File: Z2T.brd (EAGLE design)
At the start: 36 x 64 mm, 9 parts, among them J1 M02X7-SOCKET, J2 M02X6-SOCKET

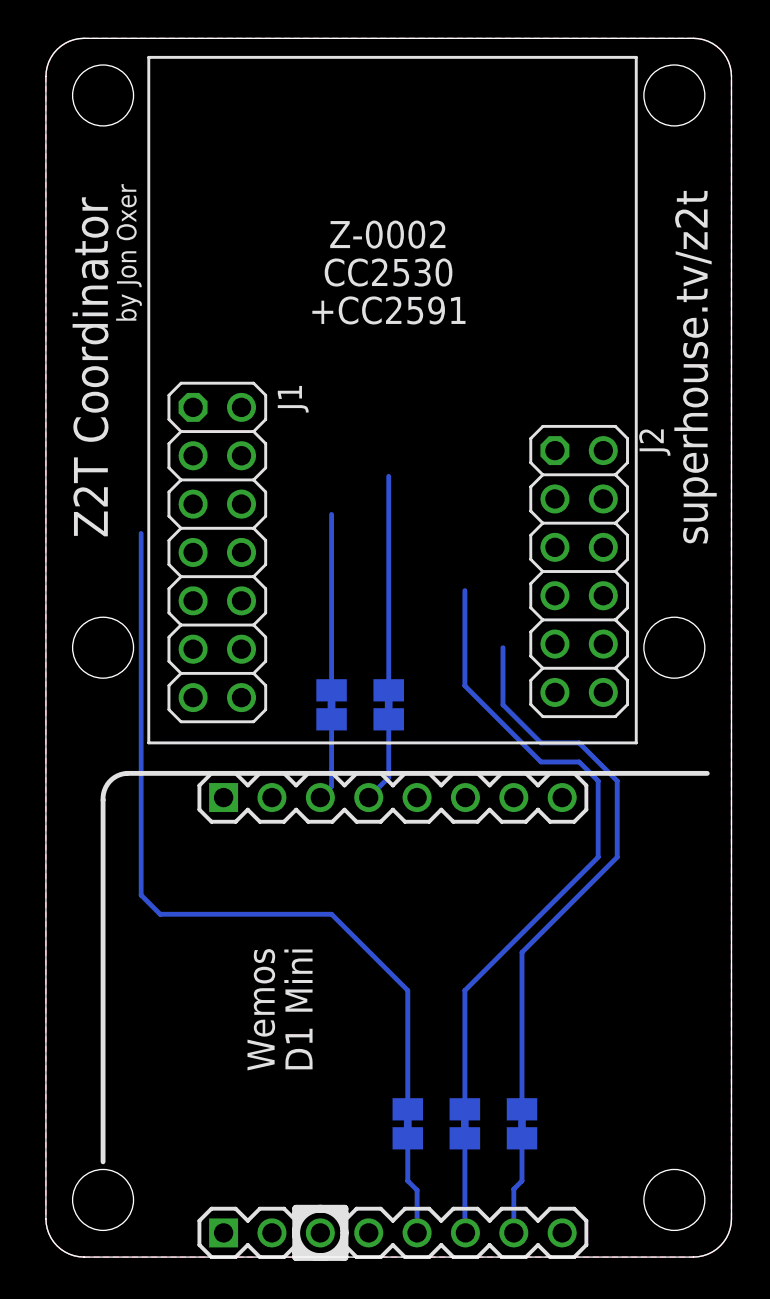
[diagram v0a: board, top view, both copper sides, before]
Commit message: Mechanical adjustments on Zigbee module
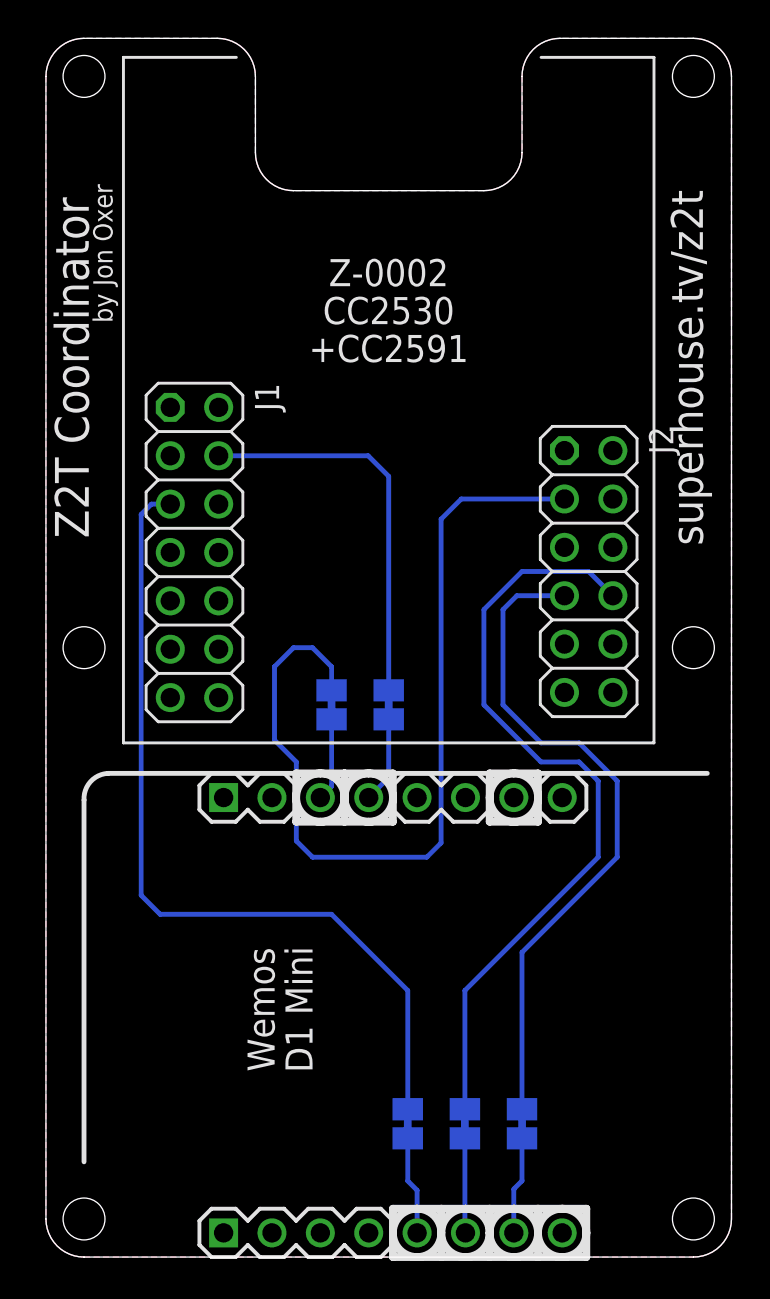
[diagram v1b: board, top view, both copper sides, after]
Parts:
- moved J1 1.20 mm to (7.80, 37.0)
- moved J2 0.50 mm to (28.5, 36.0)
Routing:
- net CC_RST: track 9.24 -> 46.9 mm
- net P2_2_DC: track 11.2 -> 20.6 mm
- net P0_3: track 34.2 -> 40.9 mm
- net P0_2: track 30.0 -> 35.5 mm
- net P2_1_DD: track 41.3 -> 44.1 mm
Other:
- outline, holes or cut-outs redrawn
- board text added: "D6: CC_DD D2: CC_DC D1: CC_RST D7: P0_3 D8: P0_2"
- board text added: "Released under the terms of the TAPR Open Hardware License: tapr.org/OHL"

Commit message: Final routing, silkscreen, DRC, and docs for v1.0 release
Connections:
- removed net 5V: J4.8
- removed net A0: J3.2
- removed net D0: J3.3
- removed net D3: J4.5
- removed net D4: J4.6
- removed net D5: J3.4
- removed net RST: J3.1
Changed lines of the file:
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@@
 <drawing>
 <settings>
-<setting alwaysvectorfont="yes"/>
+<setting alwaysvectorfont="no"/>
 <setting keepoldvectorfont="yes"/>
 <setting verticaltext="up"/>
@@
 <wire x1="18" y1="25.18" x2="18" y2="28.238" width="0.254" layer="16"/>
 </signal>
-<signal name="D5">
-<contactref element="J3" pad="4"/>
-</signal>
 <signal name="D6">
 <contactref element="J3" pad="5"/>
@@
 <wire x1="25" y1="4" x2="25" y2="6.238" width="0.254" layer="16"/>
 </signal>
-<signal name="A0">
-<contactref element="J3" pad="2"/>
-</signal>
-<signal name="D0">
-<contactref element="J3" pad="3"/>
-</signal>
-<signal name="D3">
-<contactref element="J4" pad="5"/>
-</signal>
-<signal name="D4">
-<contactref element="J4" pad="6"/>
-</signal>
 <signal name="RX">
 <contactref element="J4" pad="2"/>
@@
 <signal name="TX">
 <contactref element="J4" pad="1"/>
-</signal>
-<signal name="RST">
-<contactref element="J3" pad="1"/>
 </signal>
 <signal name="P2_3">
@@
 <contactref element="J2" pad="10"/>
 </signal>
-<signal name="5V">
-<contactref element="J4" pad="8"/>
-</signal>
 </signals>

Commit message: Fixed spacing on Zigbee module headers
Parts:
- moved J2 0.50 mm to (28.0, 36.0)
- moved J1 0.20 mm to (8.00, 37.0)
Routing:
- net P0_2: track 35.5 -> 35.0 mm
- net CC_RST: track 46.9 -> 46.4 mm
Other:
- board text added: "v1.1"
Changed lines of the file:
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@@
 <wire x1="4.07" y1="63" x2="10" y2="63" width="0.1524" layer="21"/>
 <wire x1="26" y1="63" x2="31.93" y2="63" width="0.1524" layer="21"/>
+<text x="4.712" y="7.24" size="1.27" layer="22" font="vector" ratio="18" rot="MR180" align="bottom-center">v1.1</text>
+<wire x1="35.84" y1="4.4" x2="29.73" y2="4.4" width="0.254" layer="21"/>
+<wire x1="27.84" y1="2.4" x2="29.73" y2="4.4" width="0.254" layer="21"/>
 </plain>
 <attributes>
@@
 <attribute name="VALUE" x="8.06" y="20.955" size="1.27" layer="27"/>
 </element>
-<element name="J2" library="SuperHouse-Connectors" library_urn="urn:adsk.eagle:library:11765989" package="2X06-S" package3d_urn="urn:adsk.eagle:package:15060598/2" value="M02X6-SOCKET" x="28.5" y="36" smashed="yes" rot="R270">
-<attribute name="NAME" x="31.675" y="43.62" size="1.27" layer="25" ratio="10" rot="R270"/>
-<attribute name="VALUE" x="24.055" y="43.62" size="1.27" layer="27" rot="R270"/>
-</element>
-<element name="J1" library="SuperHouse-Connectors" library_urn="urn:adsk.eagle:library:11765989" package="2X07-S" package3d_urn="urn:adsk.eagle:package:15060619/2" value="M02X7-SOCKET" x="7.8" y="37" smashed="yes" rot="R270">
-<attribute name="NAME" x="10.975" y="45.89" size="1.27" layer="25" ratio="10" rot="R270"/>
-<attribute name="VALUE" x="3.355" y="45.89" size="1.27" layer="27" rot="R270"/>
+<element name="J2" library="SuperHouse-Connectors" library_urn="urn:adsk.eagle:library:11765989" package="2X06-S" package3d_urn="urn:adsk.eagle:package:15060598/2" value="M02X6-SOCKET" x="28" y="36" smashed="yes" rot="R270">
+<attribute name="NAME" x="31.175" y="43.62" size="1.27" layer="25" ratio="10" rot="R270"/>
+<attribute name="VALUE" x="23.555" y="43.62" size="1.27" layer="27" rot="R270"/>
+</element>
+<element name="J1" library="SuperHouse-Connectors" library_urn="urn:adsk.eagle:library:11765989" package="2X07-S" package3d_urn="urn:adsk.eagle:package:15060619/2" value="M02X7-SOCKET" x="8" y="37" smashed="yes" rot="R270">
+<attribute name="NAME" x="11.175" y="45.89" size="1.27" layer="25" ratio="10" rot="R270"/>
+<attribute name="VALUE" x="3.555" y="45.89" size="1.27" layer="27" rot="R270"/>
 </element>
 <element name="SJ1" library="SuperHouse-Jumpers" library_urn="urn:adsk.eagle:library:12190622" package="SJC" package3d_urn="urn:adsk.eagle:package:7066342/1" value="SJC-NORMAL" x="19" y="7" smashed="yes" rot="MR90">
@@
 <wire x1="15" y1="18" x2="6" y2="18" width="0.254" layer="16"/>
 <wire x1="5" y1="39" x2="5.54" y2="39.54" width="0.254" layer="16"/>
-<wire x1="5.54" y1="39.54" x2="6.53" y2="39.54" width="0.254" layer="16"/>
+<wire x1="5.54" y1="39.54" x2="6.73" y2="39.54" width="0.254" layer="16"/>
 <wire x1="5" y1="19" x2="5" y2="39" width="0.254" layer="16"/>
 </signal>
@@
 <wire x1="18" y1="29.762" x2="18" y2="41" width="0.254" layer="16"/>
 <wire x1="18" y1="41" x2="16.92" y2="42.08" width="0.254" layer="16"/>
-<wire x1="16.92" y1="42.08" x2="9.07" y2="42.08" width="0.254" layer="16"/>
+<wire x1="16.92" y1="42.08" x2="9.27" y2="42.08" width="0.254" layer="16"/>
 </signal>
 <signal name="P2_4">
@@
 <wire x1="12" y1="27.15" x2="13.15" y2="26" width="0.254" layer="16"/>
 <wire x1="12" y1="31" x2="12" y2="27.15" width="0.254" layer="16"/>
-<wire x1="21.81" y1="39.81" x2="27.23" y2="39.81" width="0.254" layer="16"/>
+<wire x1="21.81" y1="39.81" x2="26.73" y2="39.81" width="0.254" layer="16"/>
 <wire x1="20.75" y1="21.75" x2="20.75" y2="38.75" width="0.254" layer="16"/>
 <wire x1="20.75" y1="38.75" x2="21.81" y2="39.81" width="0.254" layer="16"/>
@@
 <wire x1="28" y1="27" x2="26" y2="27" width="0.254" layer="16"/>
 <wire x1="24" y1="34" x2="24.73" y2="34.73" width="0.254" layer="16"/>
-<wire x1="24.73" y1="34.73" x2="27.23" y2="34.73" width="0.254" layer="16"/>
+<wire x1="24.73" y1="34.73" x2="26.73" y2="34.73" width="0.254" layer="16"/>
 <wire x1="24" y1="29" x2="24" y2="34" width="0.254" layer="16"/>
 </signal>
@@
 <wire x1="26" y1="26" x2="23" y2="29" width="0.254" layer="16"/>
 <wire x1="23" y1="34" x2="25" y2="36" width="0.254" layer="16"/>
-<wire x1="28.5" y1="36" x2="29.77" y2="34.73" width="0.254" layer="16"/>
+<wire x1="28.5" y1="36" x2="29.27" y2="34.73" width="0.254" layer="16"/>
 <wire x1="25" y1="36" x2="28.5" y2="36" width="0.254" layer="16"/>
 </signal>

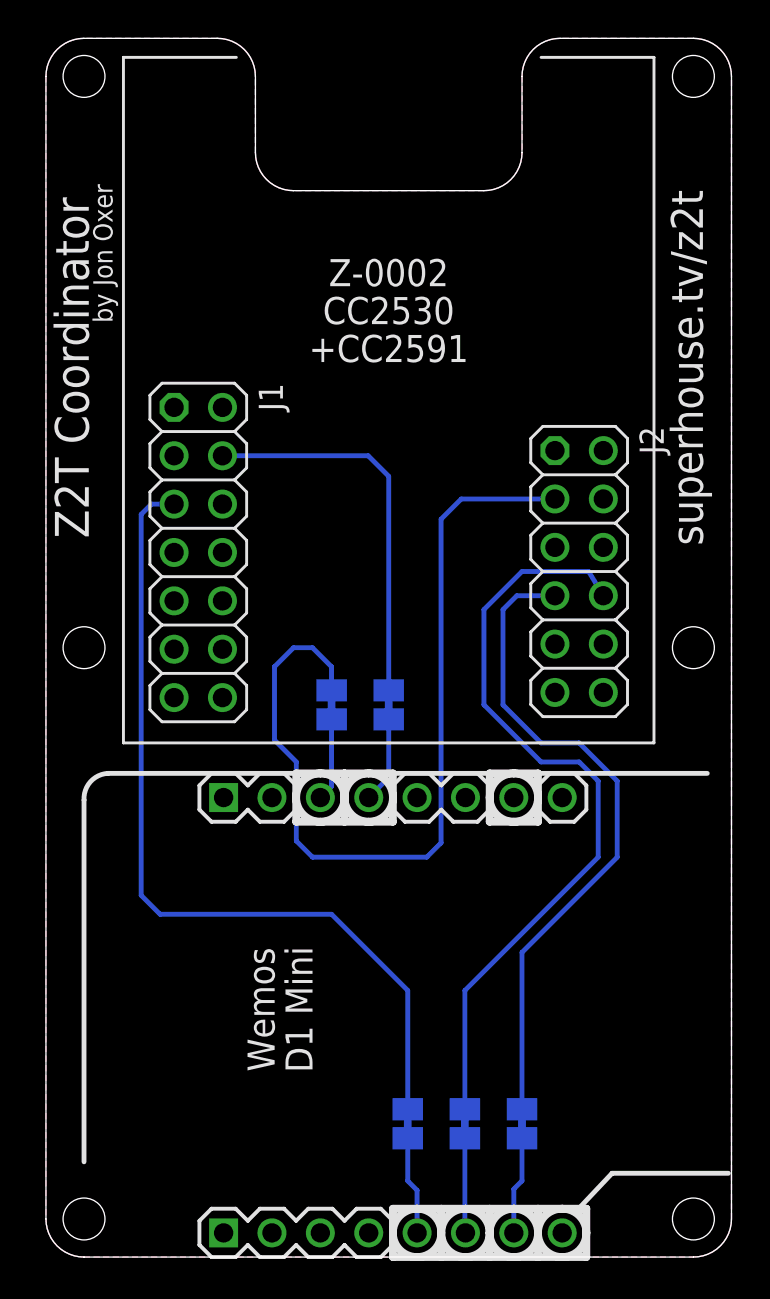
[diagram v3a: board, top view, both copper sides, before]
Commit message: Added power LED, clearance for USB socket, and pulled back copper near WiFi antenna
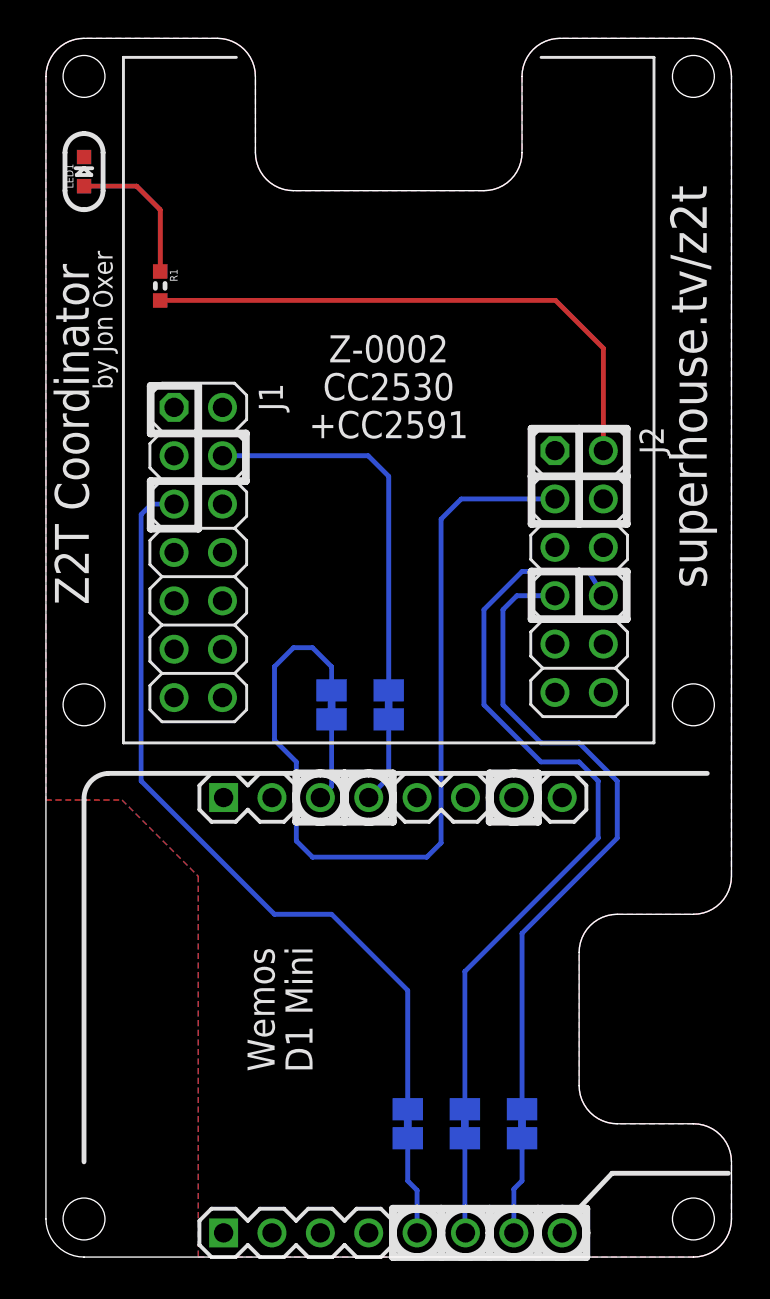
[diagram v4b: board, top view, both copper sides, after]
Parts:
- added LED1: BLUE, SuperHouse-LEDs:LED-0603
- added R1: 2K2, SuperHouse-DiscreteSemi:R0603
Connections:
- new net N$1: LED1.A, R1.1
- net 3.3V: now also R1.2
- net GND: now also LED1.C
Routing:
- net 3.3V: track 0.00 -> 29.7 mm
- net N$1: track 0.00 -> 7.75 mm
- net P2_1_DD: track 44.3 -> 40.7 mm
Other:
- outline, holes or cut-outs redrawn

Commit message: Schematic clarification, silkscreen tweaks
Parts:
- SJ1: value SJC-NORMAL -> D6/P2_1_DD
- SJ2: value SJC-NORMAL -> D2/P2_2_DC
- SJ3: value SJC-NORMAL -> D1/CC_RST
- SJ4: value SJC-NORMAL -> D7/P0_3
- SJ5: value SJC-NORMAL -> D8/P0_2
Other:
- board text added: "D6/IO12: CC_DD D2/IO4: CC_DC D1/IO5: CC_RST D7/IO13: P0_3 D8/IO15: P0_2"
- board text added: "Z-0001 CC2530 or Z-0002 CC2530 +CC2591"
- board text removed: "D6: CC_DD D2: CC_DC D1: CC_RST D7: P0_3 D8: P0_2"
- board text removed: "Z-0002 CC2530 +CC2591"
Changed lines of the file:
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@@
 <drawing>
 <settings>
-<setting alwaysvectorfont="no"/>
+<setting alwaysvectorfont="yes"/>
 <setting keepoldvectorfont="yes"/>
 <setting verticaltext="up"/>
@@
 <text x="14" y="13" size="1.4224" layer="21" font="vector" ratio="18" distance="40" rot="R90" align="bottom-center">Wemos
 D1 Mini</text>
-<text x="18" y="43" size="1.4224" layer="21" font="vector" ratio="18" distance="40" rot="SR0" align="bottom-center">Z-0002
+<text x="18" y="39" size="1.4224" layer="21" font="vector" ratio="18" distance="40" rot="SR0" align="bottom-center">Z-0001
+CC2530
+or
+Z-0002
 CC2530
 +CC2591</text>
@@
 <wire x1="13.14" y1="25.4" x2="14.41" y2="25.4" width="0.4064" layer="22"/>
 <wire x1="23.3" y1="25.4" x2="24.57" y2="25.4" width="0.4064" layer="22"/>
-<text x="23.288" y="31.76" size="1.27" layer="22" font="vector" ratio="18" rot="MR0">D6: CC_DD
-D2: CC_DC
-D1: CC_RST
-D7: P0_3
-D8: P0_2</text>
+<text x="24.8" y="33" size="1.1" layer="22" font="vector" ratio="18" rot="MR0">D6/IO12: CC_DD
+D2/IO4:  CC_DC
+D1/IO5:  CC_RST
+D7/IO13: P0_3
+D8/IO15: P0_2</text>
 <text x="14.712" y="14.24" size="1.016" layer="22" font="vector" ratio="12" distance="40" rot="MR180" align="bottom-center">Released under the terms
 of the TAPR Open Hardware
@@
 <wire x1="26" y1="63" x2="31.93" y2="63" width="0.1524" layer="21"/>
 <text x="9.712" y="8.24" size="1.27" layer="22" font="vector" ratio="18" rot="MR180" align="bottom-center">v1.1</text>
-<wire x1="35.84" y1="4.4" x2="29.73" y2="4.4" width="0.254" layer="21"/>
+<wire x1="35.84" y1="4.4" x2="33" y2="4.4" width="0.254" layer="21"/>
+<wire x1="33" y1="4.4" x2="30" y2="4.4" width="0.254" layer="21"/>
+<wire x1="30" y1="4.4" x2="29.73" y2="4.4" width="0.254" layer="21"/>
 <wire x1="27.84" y1="2.4" x2="29.73" y2="4.4" width="0.254" layer="21"/>
 <wire x1="8" y1="43.25" x2="8" y2="40.75" width="0.4064" layer="21"/>
@@
 <wire x1="3" y1="58" x2="2" y2="59" width="0.254" layer="21" curve="90"/>
 <wire x1="1" y1="58" x2="2" y2="59" width="0.254" layer="21" curve="-90"/>
+<wire x1="33" y1="4.4" x2="33" y2="4" width="0.254" layer="21"/>
+<wire x1="33" y1="4" x2="32" y2="3" width="0.254" layer="21"/>
+<wire x1="32" y1="3" x2="31" y2="3" width="0.254" layer="21"/>
+<wire x1="31" y1="3" x2="30" y2="4" width="0.254" layer="21"/>
+<wire x1="30" y1="4" x2="30" y2="4.4" width="0.254" layer="21"/>
 </plain>
 <attributes>
@@
 <attribute name="VALUE" x="3.555" y="45.89" size="1.27" layer="27" rot="R270"/>
 </element>
-<element name="SJ1" library="SuperHouse-Jumpers" library_urn="urn:adsk.eagle:library:12190622" package="SJC" package3d_urn="urn:adsk.eagle:package:7066342/1" value="SJC-NORMAL" x="19" y="7" smashed="yes" rot="MR90">
+<element name="SJ1" library="SuperHouse-Jumpers" library_urn="urn:adsk.eagle:library:12190622" package="SJC" package3d_urn="urn:adsk.eagle:package:7066342/1" value="D6/P2_1_DD" x="19" y="7" smashed="yes" rot="MR90">
 <attribute name="NAME" x="20.143" y="5.349" size="1.27" layer="26" ratio="10" rot="MR90"/>
 <attribute name="VALUE" x="19" y="7.4001" size="0.02" layer="28" rot="MR90"/>
 </element>
-<element name="SJ2" library="SuperHouse-Jumpers" library_urn="urn:adsk.eagle:library:12190622" package="SJC" package3d_urn="urn:adsk.eagle:package:7066342/1" value="SJC-NORMAL" x="18" y="29" smashed="yes" rot="MR90">
+<element name="SJ2" library="SuperHouse-Jumpers" library_urn="urn:adsk.eagle:library:12190622" package="SJC" package3d_urn="urn:adsk.eagle:package:7066342/1" value="D2/P2_2_DC" x="18" y="29" smashed="yes" rot="MR90">
 <attribute name="NAME" x="19.143" y="27.349" size="1.27" layer="26" ratio="10" rot="MR90"/>
 <attribute name="VALUE" x="18" y="29.4001" size="0.02" layer="28" rot="MR90"/>
 </element>
-<element name="SJ3" library="SuperHouse-Jumpers" library_urn="urn:adsk.eagle:library:12190622" package="SJC" package3d_urn="urn:adsk.eagle:package:7066342/1" value="SJC-NORMAL" x="15" y="29" smashed="yes" rot="MR90">
+<element name="SJ3" library="SuperHouse-Jumpers" library_urn="urn:adsk.eagle:library:12190622" package="SJC" package3d_urn="urn:adsk.eagle:package:7066342/1" value="D1/CC_RST" x="15" y="29" smashed="yes" rot="MR90">
 <attribute name="NAME" x="16.143" y="27.349" size="1.27" layer="26" ratio="10" rot="MR90"/>
 <attribute name="VALUE" x="15" y="29.4001" size="0.02" layer="28" rot="MR90"/>
 </element>
-<element name="SJ4" library="SuperHouse-Jumpers" library_urn="urn:adsk.eagle:library:12190622" package="SJC" package3d_urn="urn:adsk.eagle:package:7066342/1" value="SJC-NORMAL" x="22" y="7" smashed="yes" rot="MR90">
+<element name="SJ4" library="SuperHouse-Jumpers" library_urn="urn:adsk.eagle:library:12190622" package="SJC" package3d_urn="urn:adsk.eagle:package:7066342/1" value="D7/P0_3" x="22" y="7" smashed="yes" rot="MR90">
 <attribute name="NAME" x="23.143" y="5.349" size="1.27" layer="26" ratio="10" rot="MR90"/>
 <attribute name="VALUE" x="22" y="7.4001" size="0.02" layer="28" rot="MR90"/>
 </element>
-<element name="SJ5" library="SuperHouse-Jumpers" library_urn="urn:adsk.eagle:library:12190622" package="SJC" package3d_urn="urn:adsk.eagle:package:7066342/1" value="SJC-NORMAL" x="25" y="7" smashed="yes" rot="MR90">
+<element name="SJ5" library="SuperHouse-Jumpers" library_urn="urn:adsk.eagle:library:12190622" package="SJC" package3d_urn="urn:adsk.eagle:package:7066342/1" value="D8/P0_2" x="25" y="7" smashed="yes" rot="MR90">
 <attribute name="NAME" x="26.143" y="5.349" size="1.27" layer="26" ratio="10" rot="MR90"/>
 <attribute name="VALUE" x="25" y="7.4001" size="0.02" layer="28" rot="MR90"/>
